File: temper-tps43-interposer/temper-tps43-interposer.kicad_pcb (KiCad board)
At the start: 2 copper layers, 34 x 20 mm, 27 parts, among them CON1 TPS43 FFC

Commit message: Fix board dimensions: 34x44mm, centered to encompass all components
Board was 34x20mm - way too small. Components span from y=-17 to y=+22.
Now 34x44mm with board Y centered at 1.5mm offset.
Also fixed FFC connector pad Y to match custom footprint (1.0mm).
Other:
- board size 34 x 20 mm -> 34 x 44 mm
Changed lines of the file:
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@@
 		(attr smd)
 		(pad "1" smd rect
-			(at -1.25 0.00)
+			(at -1.25 1.00)
 			(size 0.30 1.50)
 			(layers "F.Cu" "F.Paste" "F.Mask")
@@
 		)
 		(pad "2" smd rect
-			(at -0.75 0.00)
+			(at -0.75 1.00)
 			(size 0.30 1.50)
 			(layers "F.Cu" "F.Paste" "F.Mask")
@@
 		)
 		(pad "3" smd rect
-			(at -0.25 0.00)
+			(at -0.25 1.00)
 			(size 0.30 1.50)
 			(layers "F.Cu" "F.Paste" "F.Mask")
@@
 		)
 		(pad "4" smd rect
-			(at 0.25 0.00)
+			(at 0.25 1.00)
 			(size 0.30 1.50)
 			(layers "F.Cu" "F.Paste" "F.Mask")
@@
 		)
 		(pad "5" smd rect
-			(at 0.75 0.00)
+			(at 0.75 1.00)
 			(size 0.30 1.50)
 			(layers "F.Cu" "F.Paste" "F.Mask")
@@
 		)
 		(pad "6" smd rect
-			(at 1.25 0.00)
+			(at 1.25 1.00)
 			(size 0.30 1.50)
 			(layers "F.Cu" "F.Paste" "F.Mask")
@@
 		(net 1)
 	)
-	(gr_line (start -17.00 10.00) (end 17.00 10.00) (layer "Edge.Cuts") (width 0.1))
-	(gr_line (start 17.00 10.00) (end 17.00 -10.00) (layer "Edge.Cuts") (width 0.1))
-	(gr_line (start 17.00 -10.00) (end -17.00 -10.00) (layer "Edge.Cuts") (width 0.1))
-	(gr_line (start -17.00 -10.00) (end -17.00 10.00) (layer "Edge.Cuts") (width 0.1))
-	(gr_text "Temper TPS43 Interposer" (at 0.00 8.50 0) (layer "F.SilkS") (effects (font (size 1.0 1.0) (thickness 0.15))))
-	(gr_text "v1.0" (at 0.00 7.20 0) (layer "F.SilkS") (effects (font (size 0.8 0.8) (thickness 0.15))))
+	(gr_line (start -17.00 23.50) (end 17.00 23.50) (layer "Edge.Cuts") (width 0.1))
+	(gr_line (start 17.00 23.50) (end 17.00 -20.50) (layer "Edge.Cuts") (width 0.1))
+	(gr_line (start 17.00 -20.50) (end -17.00 -20.50) (layer "Edge.Cuts") (width 0.1))
+	(gr_line (start -17.00 -20.50) (end -17.00 23.50) (layer "Edge.Cuts") (width 0.1))
+	(gr_text "Temper TPS43 Interposer" (at 0.00 22.00 0) (layer "F.SilkS") (effects (font (size 1.0 1.0) (thickness 0.15))))
+	(gr_text "v1.0" (at 0.00 20.70 0) (layer "F.SilkS") (effects (font (size 0.8 0.8) (thickness 0.15))))
 	(gr_text "SDA(2)   SCL(3)   RDY(4)   RST(5)" (at 0.00 13.20 0) (layer "F.SilkS") (effects (font (size 0.8 0.8) (thickness 0.15))))
 	(gr_text "VCC(1)                     GND(6)" (at 0.00 11.90 0) (layer "F.SilkS") (effects (font (size 0.6 0.6) (thickness 0.15))))

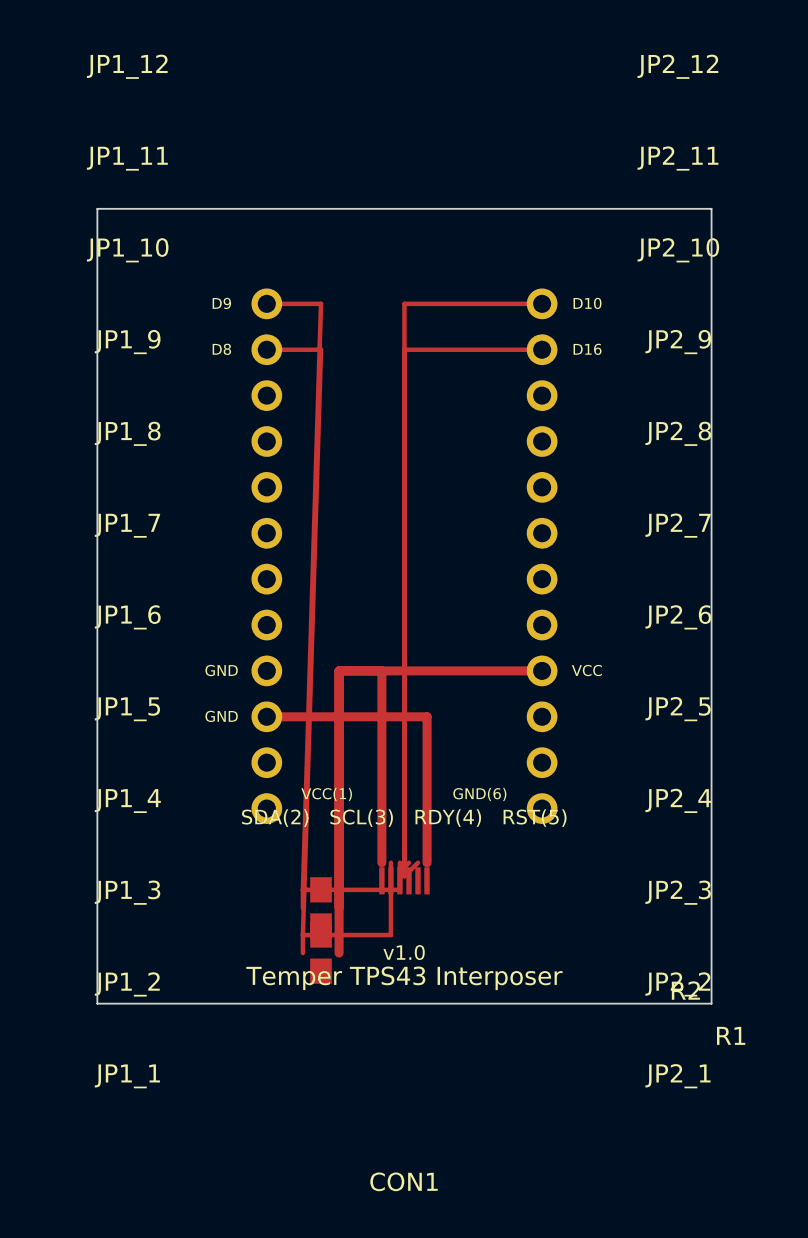
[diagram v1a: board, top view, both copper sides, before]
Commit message: Rewrite: use 1x12 pin headers (JP1, JP2), no auto-routed tracks
- JP1 and JP2 are proper 12-pin headers with clean reference designators
- FFC connector (CON1) and resistors (R1, R2) pre-placed
- Nets pre-assigned on all pads
- No crude auto-routed tracks — use KiCad interactive router instead
- Board 34x44mm, properly sized for all components
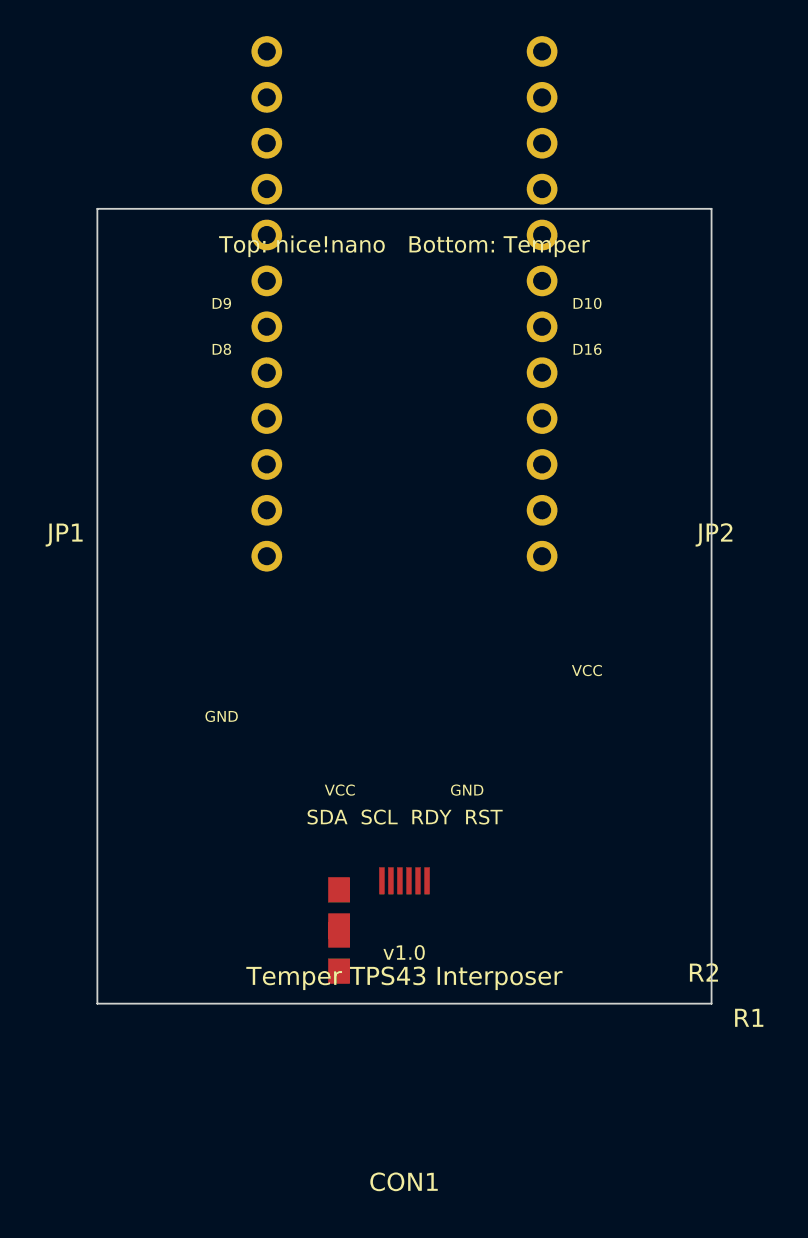
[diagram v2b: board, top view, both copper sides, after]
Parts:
- removed JP1_1: D1, Connector_PinHeader_2.54mm:PinHeader_1x01_P2.54mm_Vertical
- removed JP1_10: D7, Connector_PinHeader_2.54mm:PinHeader_1x01_P2.54mm_Vertical
- removed JP1_11: D8, Connector_PinHeader_2.54mm:PinHeader_1x01_P2.54mm_Vertical
- removed JP1_12: D9, Connector_PinHeader_2.54mm:PinHeader_1x01_P2.54mm_Vertical
- removed JP1_2: D0, Connector_PinHeader_2.54mm:PinHeader_1x01_P2.54mm_Vertical
- removed JP1_3, JP1_4, JP2_2: GND, Connector_PinHeader_2.54mm:PinHeader_1x01_P2.54mm_Vertical
- removed JP1_5: D2, Connector_PinHeader_2.54mm:PinHeader_1x01_P2.54mm_Vertical
- removed JP1_6: D3, Connector_PinHeader_2.54mm:PinHeader_1x01_P2.54mm_Vertical
- removed JP1_7: D4, Connector_PinHeader_2.54mm:PinHeader_1x01_P2.54mm_Vertical
- removed JP1_8: D5, Connector_PinHeader_2.54mm:PinHeader_1x01_P2.54mm_Vertical
- removed JP1_9: D6, Connector_PinHeader_2.54mm:PinHeader_1x01_P2.54mm_Vertical
- removed JP2_1: RAW, Connector_PinHeader_2.54mm:PinHeader_1x01_P2.54mm_Vertical
- removed JP2_10: D14, Connector_PinHeader_2.54mm:PinHeader_1x01_P2.54mm_Vertical
- removed JP2_11: D16, Connector_PinHeader_2.54mm:PinHeader_1x01_P2.54mm_Vertical
- removed JP2_12: D10, Connector_PinHeader_2.54mm:PinHeader_1x01_P2.54mm_Vertical
- removed JP2_3: RST, Connector_PinHeader_2.54mm:PinHeader_1x01_P2.54mm_Vertical
- removed JP2_4: VCC, Connector_PinHeader_2.54mm:PinHeader_1x01_P2.54mm_Vertical
- removed JP2_5: D21, Connector_PinHeader_2.54mm:PinHeader_1x01_P2.54mm_Vertical
- removed JP2_6: D20, Connector_PinHeader_2.54mm:PinHeader_1x01_P2.54mm_Vertical
- removed JP2_7: D19, Connector_PinHeader_2.54mm:PinHeader_1x01_P2.54mm_Vertical
- removed JP2_8: D18, Connector_PinHeader_2.54mm:PinHeader_1x01_P2.54mm_Vertical
- removed JP2_9: D15, Connector_PinHeader_2.54mm:PinHeader_1x01_P2.54mm_Vertical
- added JP1: ProMicro Left, Connector_PinHeader_2.54mm:PinHeader_1x12_P2.54mm_Vertical, F.Cu at (-7.62, -1.27)
- added JP2: ProMicro Right, Connector_PinHeader_2.54mm:PinHeader_1x12_P2.54mm_Vertical, F.Cu at (7.62, -1.27)
- moved R1 1.00 mm to (-3.62, 20.7)
- moved R2 1.00 mm to (-3.62, 18.2)
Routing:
- net VCC: track 53.0 -> 0.00 mm
- net SDA: track 45.3 -> 0.00 mm
- net SCL: track 43.3 -> 0.00 mm
- net RDY: track 39.2 -> 0.00 mm
- net RST: track 37.8 -> 0.00 mm
- net GND: track 16.9 -> 0.00 mm
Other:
- board text added: "SDA SCL RDY RST"
- board text added: "Top: nice!nano Bottom: Temper"
- board text added: "VCC GND"
- board text removed: "SDA(2) SCL(3) RDY(4) RST(5)"
- board text removed: "VCC(1) GND(6)"
